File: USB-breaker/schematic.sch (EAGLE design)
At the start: 17 parts, among them K1 G6K-2P, K3 G6K-2P, X1 PN87520-S, X2 PN87520-S

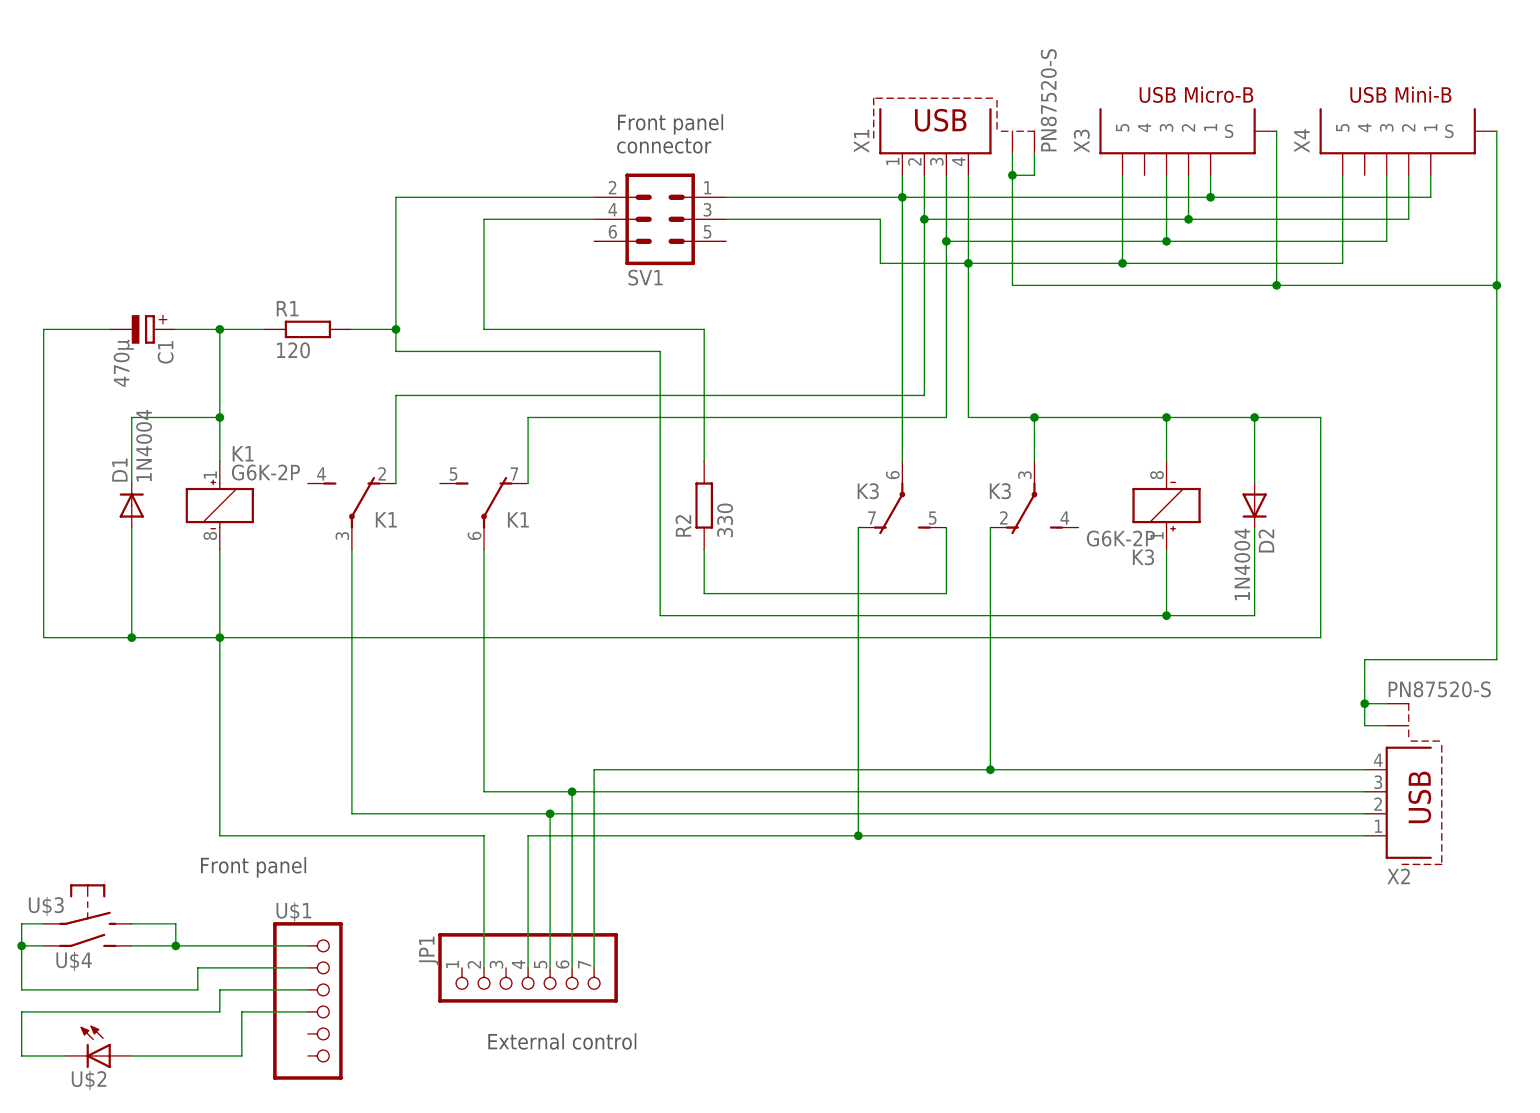
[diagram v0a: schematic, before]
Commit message: Switching of the relays is done upstream with transistors.
Also finished connecting nets to the external interface connector.
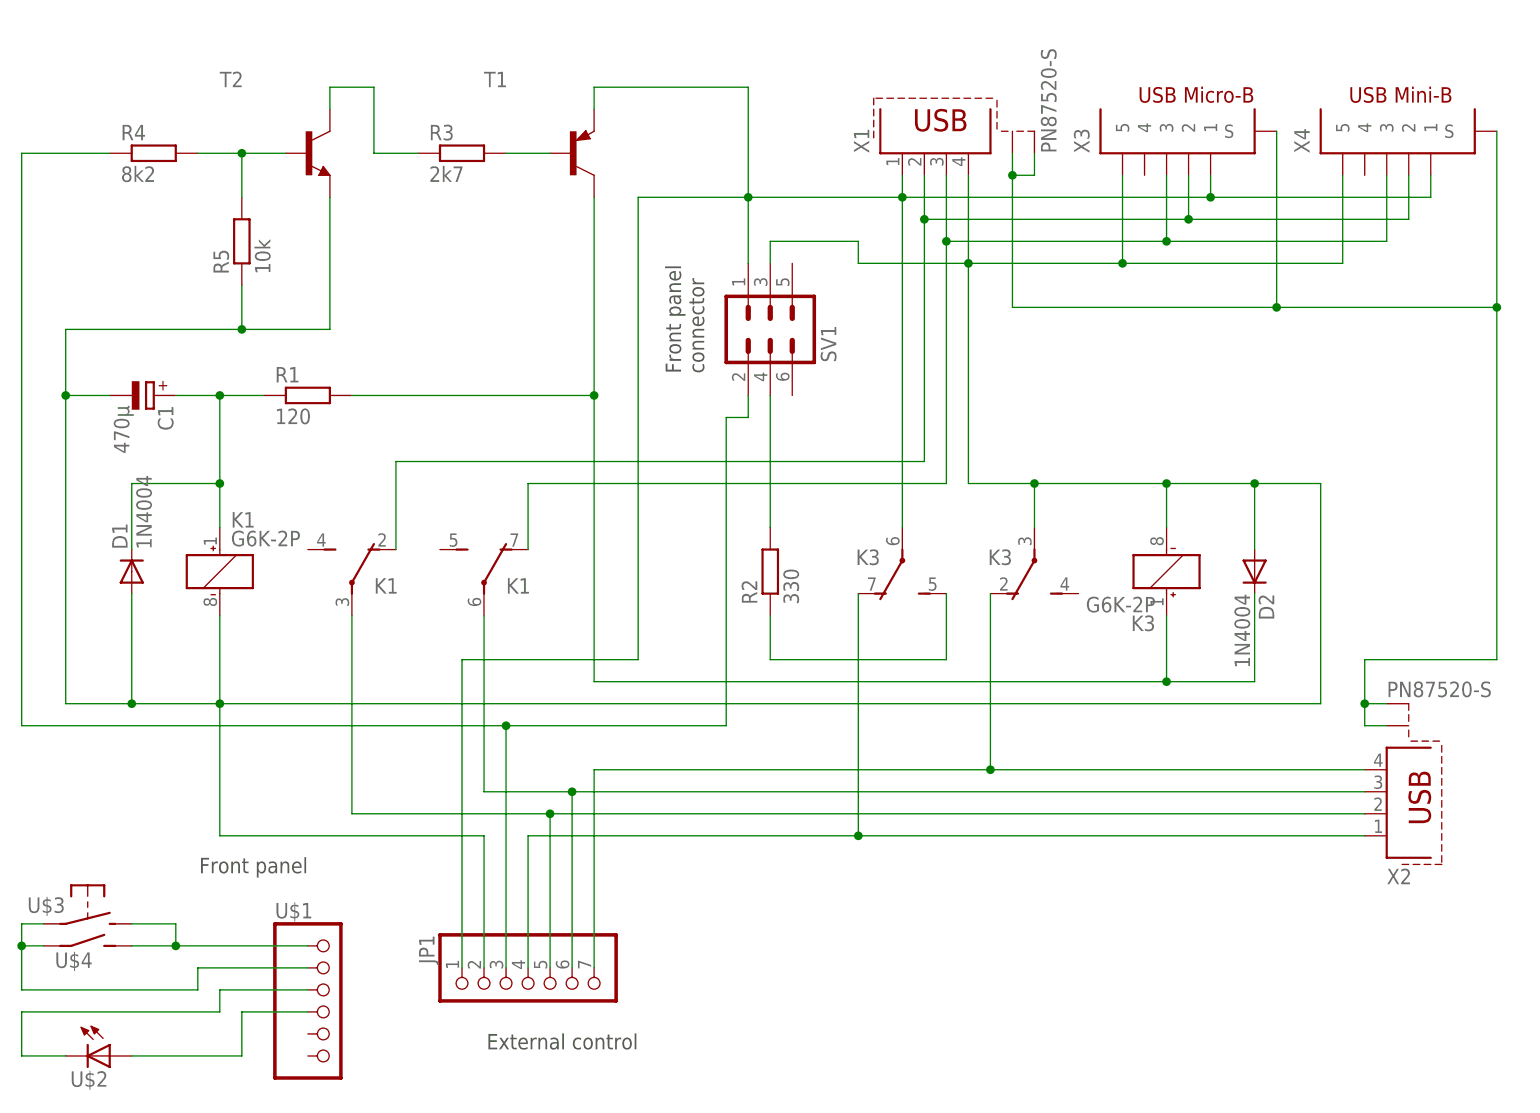
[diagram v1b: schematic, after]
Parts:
- added R3: 2k7, resistor:R-EU_0207/10
- added R4: 8k2, resistor:R-EU_0207/10
- added R5: 10k, resistor:R-EU_0207/10
- added T1: (no value), transistor:BC558B-PNP-TO92-EBC
- added T2: (no value), transistor:BC548-NPN-TO92-CBE
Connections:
- new net EXTERNAL_ENABLE: JP1.3, R4.1, SV1.2, U$1.2, U$3.P, U$4.1
- new net N$1: R3.2, T1.B
- new net N$2: R3.1, T2.C
- new net N$3: R4.2, R5.2, T2.B
- net ENABLE: now also T1.C; no longer SV1.2, U$1.2, U$3.P, U$4.1
- net GND_IN: now also R5.1, T2.E
- net VCC_IN: now also JP1.1, T1.E
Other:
- moved on the sheet: C1, D1, D2, K1, K3, R1, R2, SV1

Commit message: The schematic is now pretty much done:
- Library update
- Values for the two transistors
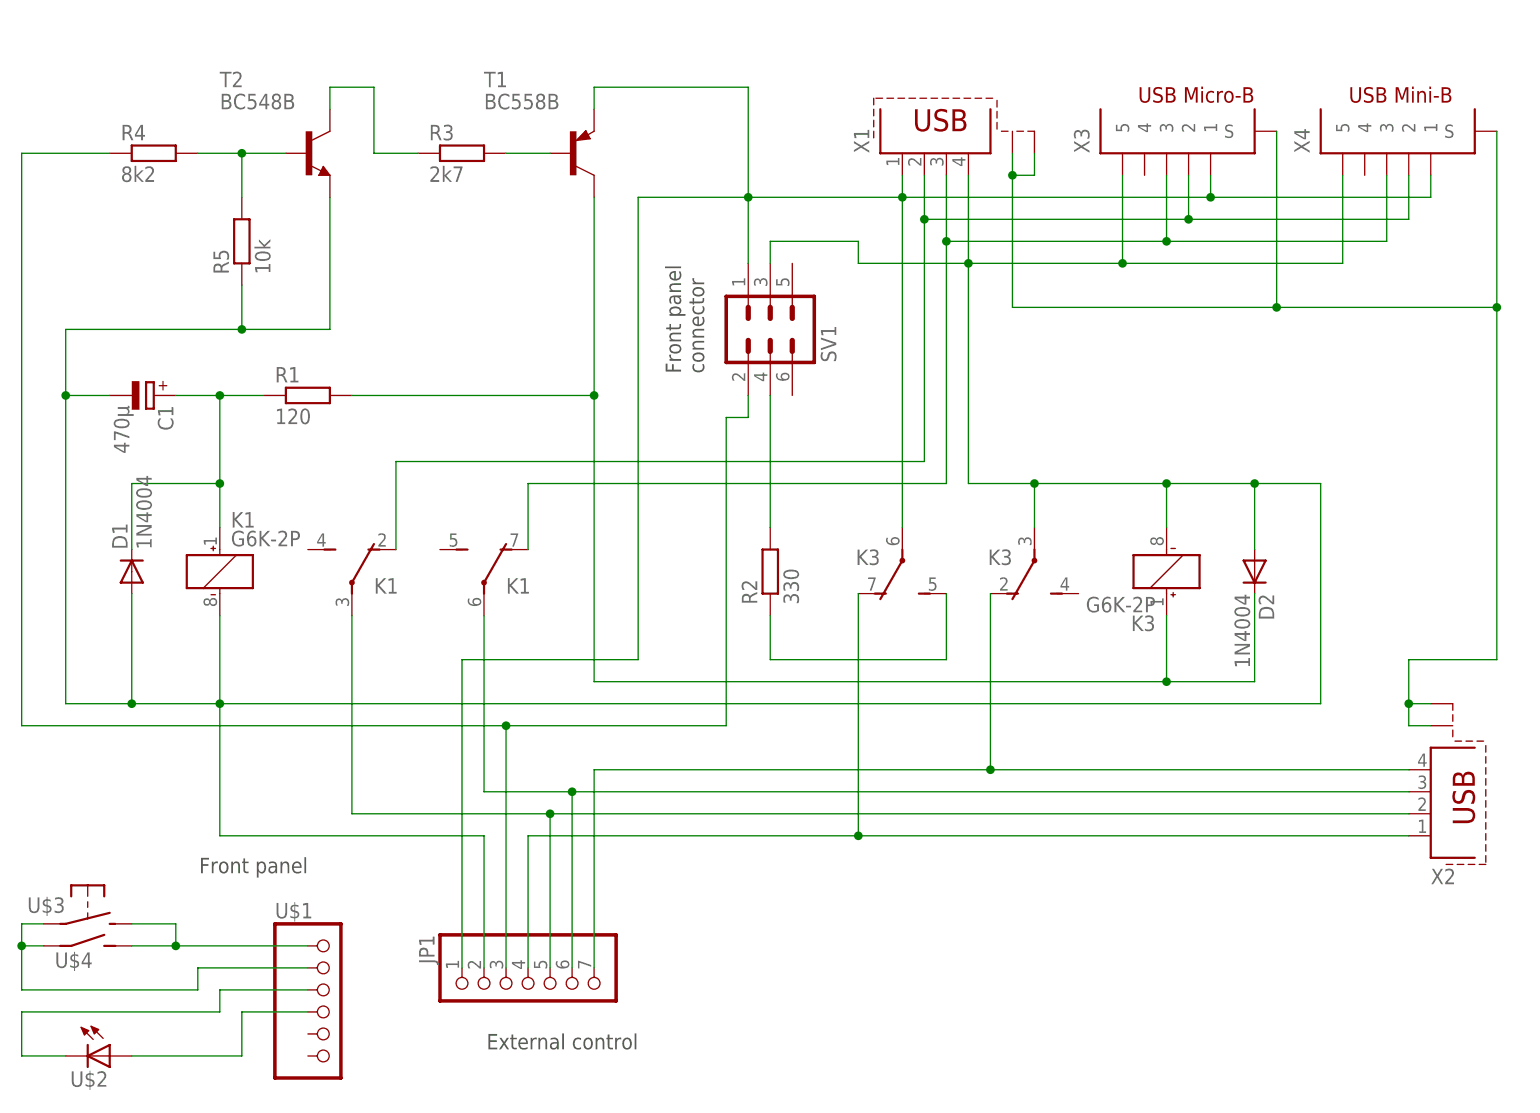
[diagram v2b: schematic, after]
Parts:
- T1: value (none) -> BC558B
- T2: value (none) -> BC548B
- X3: value (none) -> 10104110
- X4: value (none) -> UX60SC-MB-5ST
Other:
- moved on the sheet: X2
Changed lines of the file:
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@@
 <setting verticaltext="up"/>
 </settings>
-<grid distance="0.1" unitdist="inch" unit="inch" style="lines" multiple="1" display="yes" altdistance="0.01" altunitdist="inch" altunit="inch"/>
+<grid distance="0.1" unitdist="inch" unit="inch" style="lines" multiple="1" display="no" altdistance="0.01" altunitdist="inch" altunit="inch"/>
 <layers>
 <layer number="1" name="Top" color="4" fill="1" visible="no" active="no"/>
@@
 <part name="U$4" library="mibe" deviceset="EXTERNAL_SWITCH" device=""/>
 <part name="JP1" library="pinhead" deviceset="PINHD-1X7" device="/90"/>
-<part name="T1" library="transistor" deviceset="*-PNP-" device="TO92-EBC" technology="BC558B"/>
+<part name="T1" library="transistor" deviceset="*-PNP-" device="TO92-EBC" technology="BC558B" value="BC558B"/>
 <part name="R3" library="resistor" deviceset="R-EU_" device="0207/10" value="2k7"/>
-<part name="T2" library="transistor" deviceset="*-NPN-" device="TO92-CBE" technology="BC548"/>
+<part name="T2" library="transistor" deviceset="*-NPN-" device="TO92-CBE" technology="BC548" value="BC548B"/>
 <part name="R4" library="resistor" deviceset="R-EU_" device="0207/10" value="8k2"/>
 <part name="R5" library="resistor" deviceset="R-EU_" device="0207/10" value="10k"/>
@@
 <instance part="K3" gate="2" x="124.46" y="68.58" rot="R180"/>
 <instance part="K3" gate="3" x="109.22" y="68.58" rot="R180"/>
-<instance part="X3" gate="G$1" x="144.78" y="121.92" rot="R90"/>
-<instance part="X4" gate="G$1" x="170.18" y="121.92" rot="R90"/>
-<instance part="X2" gate="G$1" x="165.1" y="40.64" rot="MR180"/>
-<instance part="X1" gate="G$1" x="114.3" y="114.3" rot="R90"/>
+<instance part="X3" gate="G$1" x="144.78" y="121.92" smashed="yes" rot="R90">
+<attribute name="NAME" x="130.81" y="114.3" size="1.778" layer="95" rot="R90"/>
+</instance>
+<instance part="X4" gate="G$1" x="170.18" y="121.92" smashed="yes" rot="R90">
+<attribute name="NAME" x="156.21" y="114.3" size="1.778" layer="95" rot="R90"/>
+</instance>
+<instance part="X2" gate="G$1" x="170.18" y="40.64" smashed="yes" rot="MR180">
+<attribute name="NAME" x="170.18" y="31.75" size="1.778" layer="95" rot="MR180"/>
+</instance>
+<instance part="X1" gate="G$1" x="114.3" y="114.3" smashed="yes" rot="R90">
+<attribute name="NAME" x="105.41" y="114.3" size="1.778" layer="95" rot="R90"/>
+</instance>
 <instance part="SV1" gate="1" x="93.98" y="93.98" rot="MR90"/>
 <instance part="U$1" gate="G$1" x="43.18" y="15.24" smashed="yes">
@@
 <net name="VCC_OUT" class="0">
 <segment>
-<wire x1="104.14" y1="35.56" x2="162.56" y2="35.56" width="0.1524" layer="91"/>
+<wire x1="104.14" y1="35.56" x2="167.64" y2="35.56" width="0.1524" layer="91"/>
 <wire x1="104.14" y1="63.5" x2="104.14" y2="35.56" width="0.1524" layer="91"/>
 <pinref part="K3" gate="3" pin="O"/>
@@
 <wire x1="60.96" y1="40.64" x2="71.12" y2="40.64" width="0.1524" layer="91"/>
 <pinref part="K1" gate="3" pin="P"/>
-<wire x1="71.12" y1="40.64" x2="162.56" y2="40.64" width="0.1524" layer="91"/>
+<wire x1="71.12" y1="40.64" x2="167.64" y2="40.64" width="0.1524" layer="91"/>
 <wire x1="60.96" y1="60.96" x2="60.96" y2="40.64" width="0.1524" layer="91"/>
 <pinref part="X2" gate="G$1" pin="3"/>
@@
 <wire x1="45.72" y1="38.1" x2="68.58" y2="38.1" width="0.1524" layer="91"/>
 <pinref part="K1" gate="2" pin="P"/>
-<wire x1="68.58" y1="38.1" x2="162.56" y2="38.1" width="0.1524" layer="91"/>
+<wire x1="68.58" y1="38.1" x2="167.64" y2="38.1" width="0.1524" layer="91"/>
 <wire x1="45.72" y1="60.96" x2="45.72" y2="38.1" width="0.1524" layer="91"/>
 <pinref part="X2" gate="G$1" pin="2"/>
@@
 <wire x1="177.8" y1="96.52" x2="177.8" y2="55.88" width="0.1524" layer="91"/>
 <junction x="177.8" y="96.52"/>
-<wire x1="177.8" y1="55.88" x2="162.56" y2="55.88" width="0.1524" layer="91"/>
-<wire x1="162.56" y1="55.88" x2="162.56" y2="50.8" width="0.1524" layer="91"/>
+<wire x1="177.8" y1="55.88" x2="167.64" y2="55.88" width="0.1524" layer="91"/>
+<wire x1="167.64" y1="55.88" x2="167.64" y2="50.8" width="0.1524" layer="91"/>
 <pinref part="X2" gate="G$1" pin="S2"/>
-<wire x1="162.56" y1="50.8" x2="165.1" y2="50.8" width="0.1524" layer="91"/>
-<wire x1="162.56" y1="50.8" x2="162.56" y2="48.26" width="0.1524" layer="91"/>
-<junction x="162.56" y="50.8"/>
+<wire x1="167.64" y1="50.8" x2="170.18" y2="50.8" width="0.1524" layer="91"/>
+<wire x1="167.64" y1="50.8" x2="167.64" y2="48.26" width="0.1524" layer="91"/>
+<junction x="167.64" y="50.8"/>
 <pinref part="X2" gate="G$1" pin="S1"/>
-<wire x1="162.56" y1="48.26" x2="165.1" y2="48.26" width="0.1524" layer="91"/>
+<wire x1="167.64" y1="48.26" x2="170.18" y2="48.26" width="0.1524" layer="91"/>
 </segment>
 </net>
@@
 <segment>
 <pinref part="X2" gate="G$1" pin="4"/>
-<wire x1="119.38" y1="43.18" x2="162.56" y2="43.18" width="0.1524" layer="91"/>
+<wire x1="119.38" y1="43.18" x2="167.64" y2="43.18" width="0.1524" layer="91"/>
 <pinref part="K3" gate="2" pin="O"/>
 <wire x1="119.38" y1="63.5" x2="119.38" y2="43.18" width="0.1524" layer="91"/>

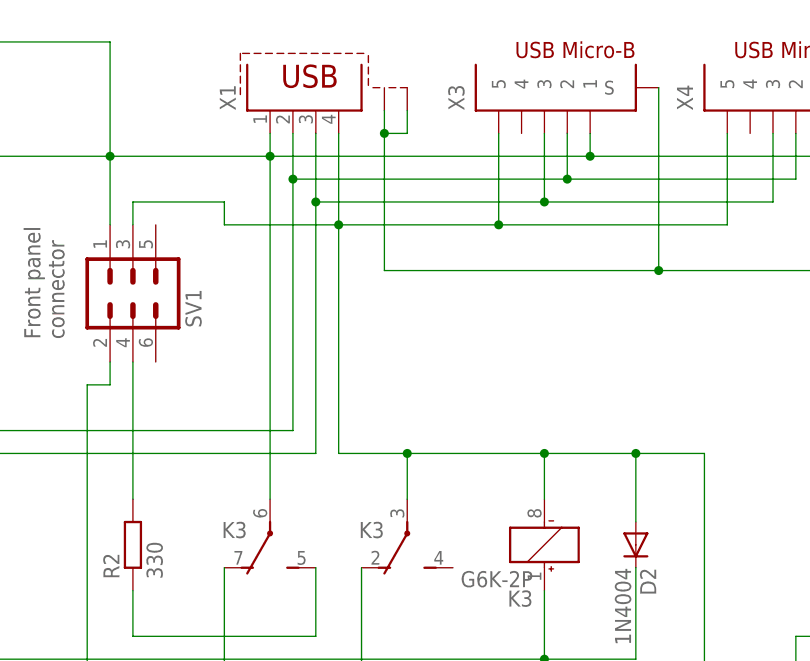
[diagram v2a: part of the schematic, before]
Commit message: Added some capacitance on VBUS, per USB spec. 7.2.4.1 / table 7-7.
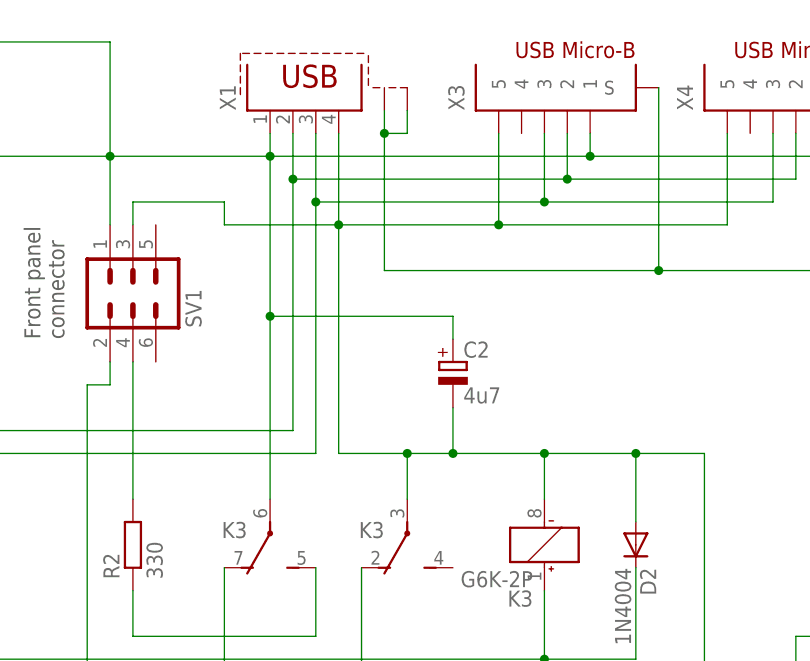
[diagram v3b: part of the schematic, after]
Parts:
- added C2: 4u7, resistor:CPOL-EUE2.5-6
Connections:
- net GND_IN: now also C2.-
- net VCC_IN: now also C2.+
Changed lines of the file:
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@@
 <part name="R4" library="resistor" deviceset="R-EU_" device="0207/10" value="8k2"/>
 <part name="R5" library="resistor" deviceset="R-EU_" device="0207/10" value="10k"/>
+<part name="C2" library="resistor" deviceset="CPOL-EU" device="E2.5-6" value="4u7"/>
 </parts>
 <sheets>
@@
 <instance part="R4" gate="G$1" x="22.86" y="114.3"/>
 <instance part="R5" gate="G$1" x="33.02" y="104.14" rot="R90"/>
+<instance part="C2" gate="G$1" x="129.54" y="86.36"/>
 </instances>
 <busses>
@@
 <segment>
 <wire x1="109.22" y1="111.76" x2="109.22" y2="109.22" width="0.1524" layer="91"/>
-<wire x1="109.22" y1="109.22" x2="109.22" y2="71.12" width="0.1524" layer="91"/>
+<wire x1="109.22" y1="109.22" x2="109.22" y2="91.44" width="0.1524" layer="91"/>
 <junction x="109.22" y="109.22"/>
 <pinref part="K3" gate="3" pin="P"/>
 <pinref part="X3" gate="G$1" pin="1"/>
+<wire x1="109.22" y1="91.44" x2="109.22" y2="71.12" width="0.1524" layer="91"/>
 <wire x1="109.22" y1="109.22" x2="144.78" y2="109.22" width="0.1524" layer="91"/>
 <wire x1="144.78" y1="109.22" x2="144.78" y2="111.76" width="0.1524" layer="91"/>
@@
 <pinref part="JP1" gate="A" pin="1"/>
 <wire x1="58.42" y1="55.88" x2="58.42" y2="20.32" width="0.1524" layer="91"/>
+<pinref part="C2" gate="G$1" pin="+"/>
+<wire x1="129.54" y1="88.9" x2="129.54" y2="91.44" width="0.1524" layer="91"/>
+<wire x1="129.54" y1="91.44" x2="109.22" y2="91.44" width="0.1524" layer="91"/>
+<junction x="109.22" y="91.44"/>
 </segment>
 <segment>
@@
 <wire x1="116.84" y1="76.2" x2="124.46" y2="76.2" width="0.1524" layer="91"/>
 <wire x1="124.46" y1="76.2" x2="124.46" y2="71.12" width="0.1524" layer="91"/>
-<wire x1="124.46" y1="76.2" x2="139.7" y2="76.2" width="0.1524" layer="91"/>
+<wire x1="124.46" y1="76.2" x2="129.54" y2="76.2" width="0.1524" layer="91"/>
 <junction x="124.46" y="76.2"/>
+<wire x1="129.54" y1="76.2" x2="139.7" y2="76.2" width="0.1524" layer="91"/>
 <wire x1="139.7" y1="76.2" x2="139.7" y2="71.12" width="0.1524" layer="91"/>
 <wire x1="139.7" y1="76.2" x2="149.86" y2="76.2" width="0.1524" layer="91"/>
@@
 <wire x1="12.7" y1="93.98" x2="33.02" y2="93.98" width="0.1524" layer="91"/>
 <junction x="33.02" y="93.98"/>
+<pinref part="C2" gate="G$1" pin="-"/>
+<wire x1="129.54" y1="81.28" x2="129.54" y2="76.2" width="0.1524" layer="91"/>
+<junction x="129.54" y="76.2"/>
 </segment>
 <segment>
